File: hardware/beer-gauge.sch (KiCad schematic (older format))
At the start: 19 parts, among them J1 OLED_MODULE, P1 CONN_01X04, P2 CONN_01X04, P3 CONN_01X04, P4 CONN_01X04, U1 ADS1234IPW

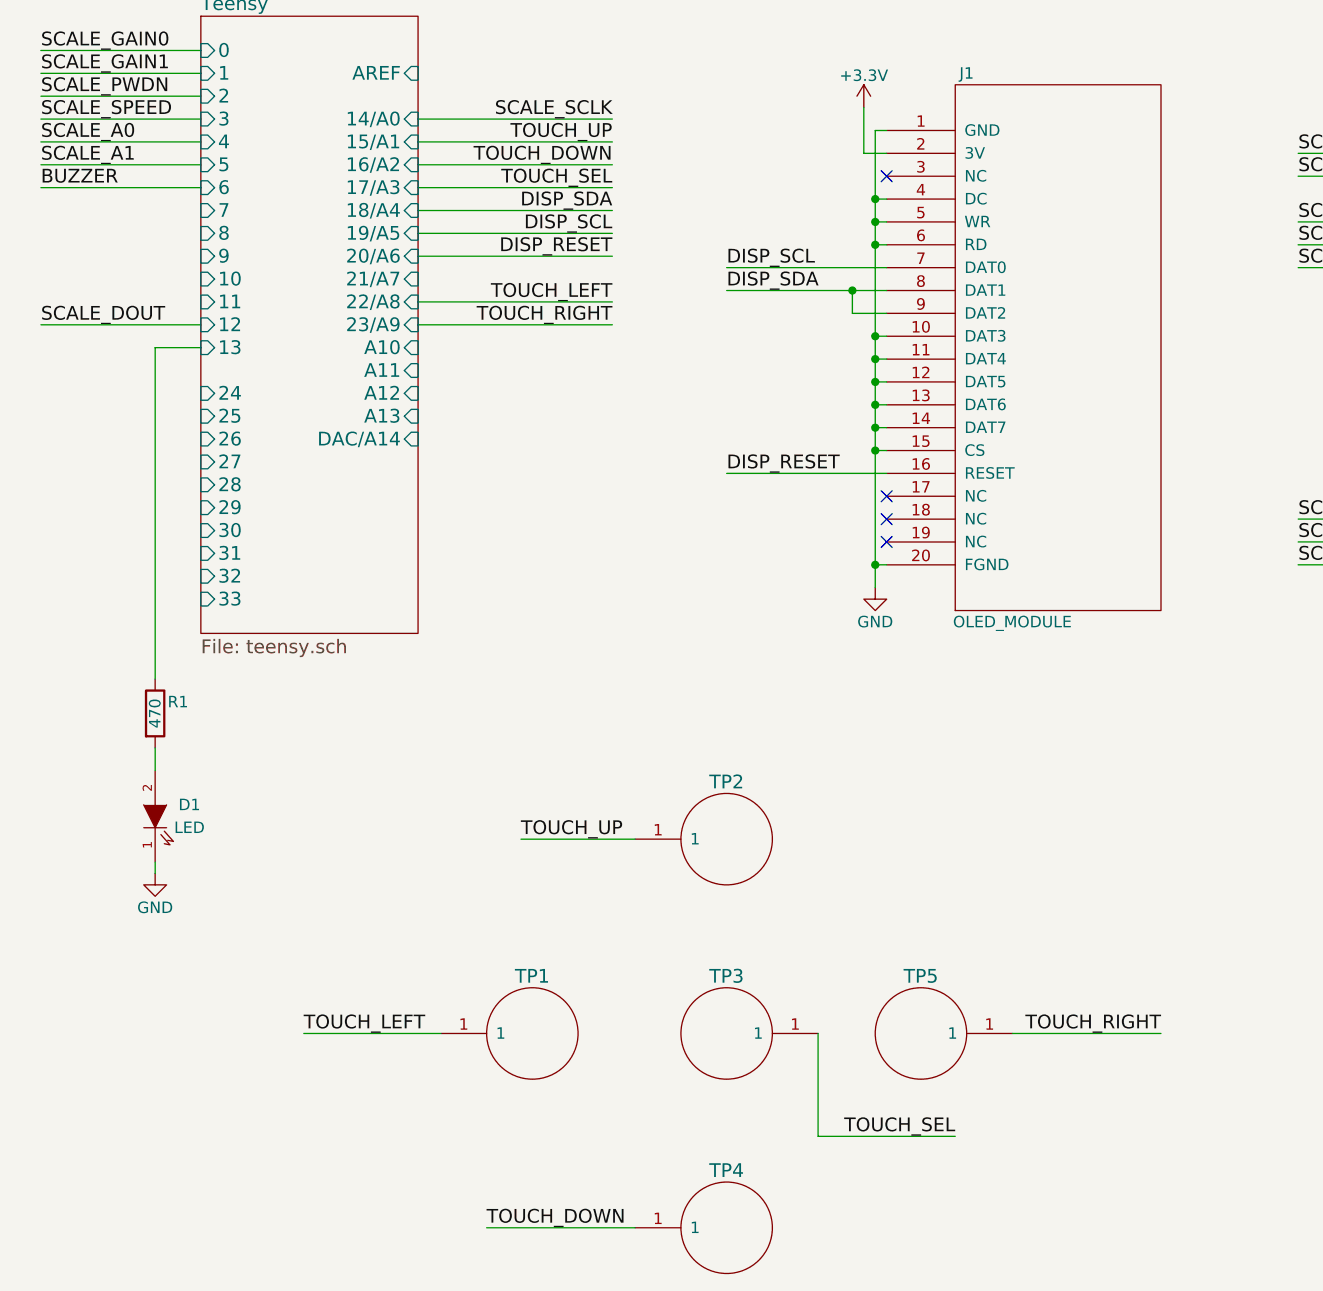
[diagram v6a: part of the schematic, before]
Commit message: Working on capacitive touch pad.  Added footprint for piezo
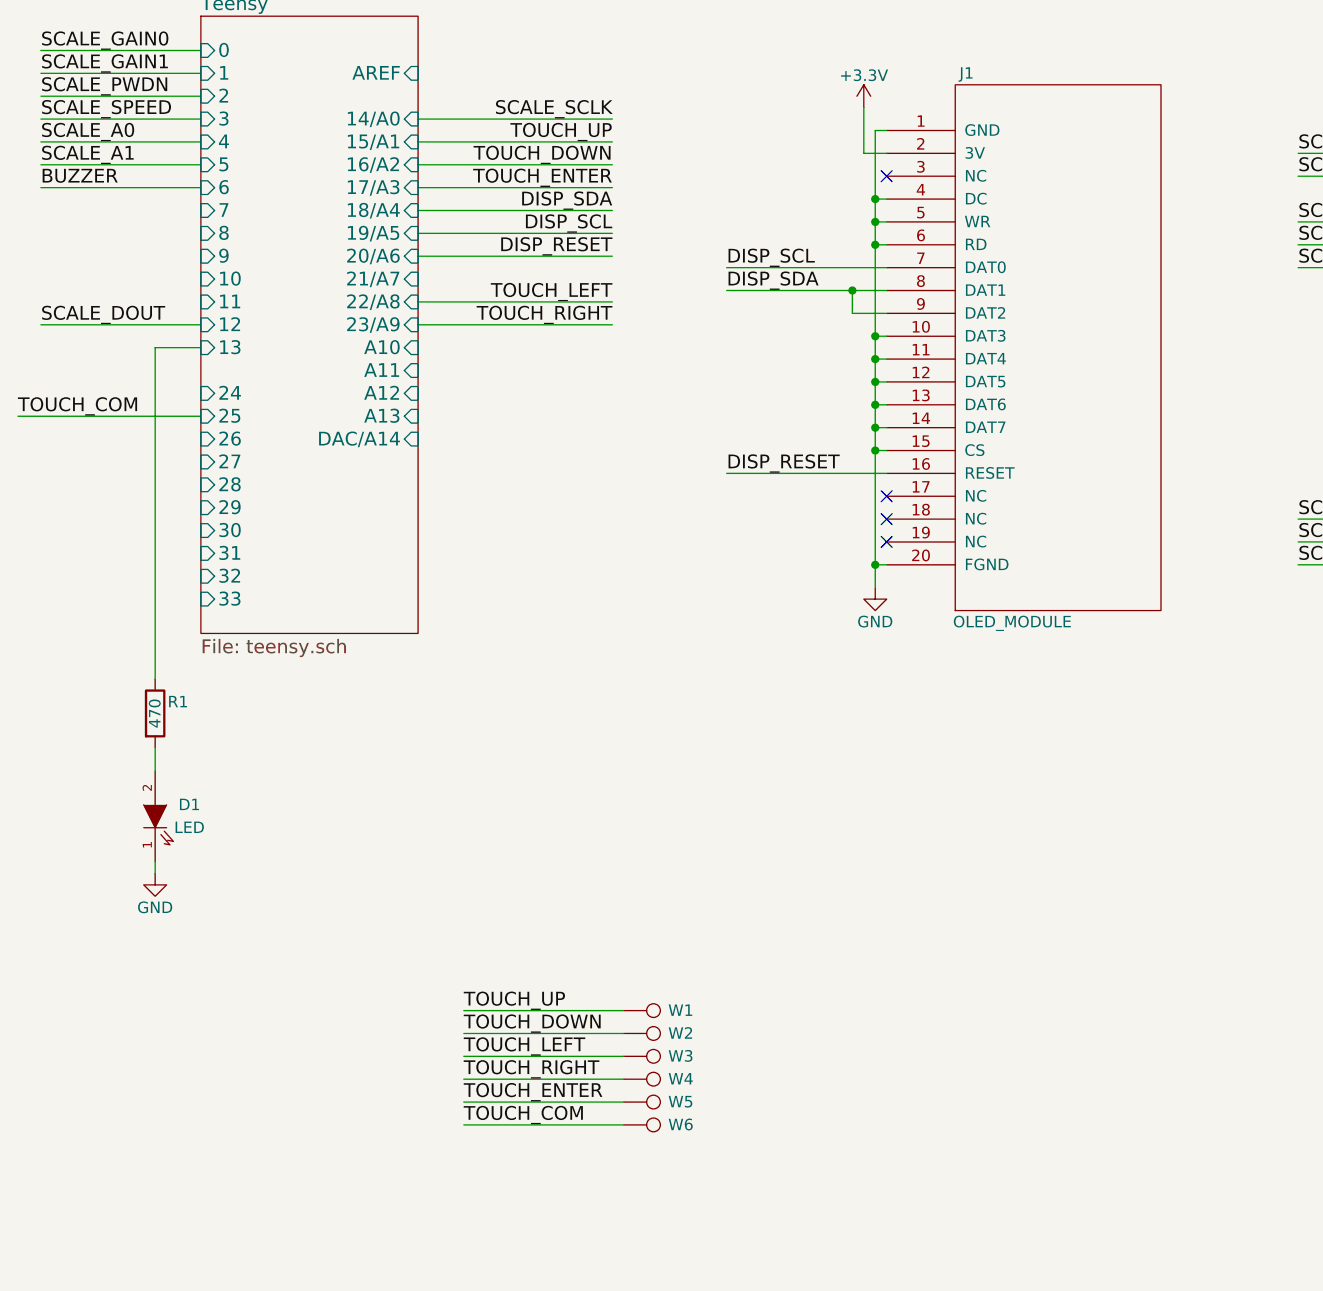
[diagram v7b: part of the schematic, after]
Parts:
- removed TP1, TP2, TP3, TP4, TP5: TOUCH_PAD, symbol TOUCH_PAD
- added W1, W2, W3, W4, W5, W6: TEST_1P, Measurement_Points:Measurement_Point_Round-TH_Small, symbol TEST_1P
- R5: footprint (none) -> Resistors_SMD:R_0603
- SP1: footprint (none) -> footprint:PKMCS
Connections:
- net TOUCH_DOWN: now also W2.1
- net TOUCH_LEFT: now also W3.1
- net TOUCH_RIGHT: now also W4.1
- net TOUCH_UP: now also W1.1
- new net TOUCH_COM: W6.1
- new net TOUCH_ENTER: W5.1
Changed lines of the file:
@@
 Text Label 3600 2650 2    60   ~ 0
 DISP_SDA
-Text Label 2250 6250 0    60   ~ 0
+Text Label 2950 6350 0    60   ~ 0
 TOUCH_LEFT
-Text Label 6000 6250 2    60   ~ 0
+Text Label 2950 6450 0    60   ~ 0
 TOUCH_RIGHT
-Text Label 3200 5400 0    60   ~ 0
+Text Label 2950 6150 0    60   ~ 0
 TOUCH_UP
-Text Label 3050 7100 0    60   ~ 0
+Text Label 2950 6250 0    60   ~ 0
 TOUCH_DOWN
 Text Label 3600 2350 2    60   ~ 0
@@
 Text Label 3600 3150 2    60   ~ 0
 TOUCH_RIGHT
-Text Label 3600 2550 2    60   ~ 0
-TOUCH_SEL
 $Sheet
 S 1800 1800 950  2700
@@
 $EndSheet
 $Comp
-L TOUCH_PAD TP1
-U 1 1 576569ED
-P 3250 6250
-F 0 "TP1" H 3250 6500 60  0000 C CNN
-F 1 "TOUCH_PAD" H 3300 5950 60  0001 C CNN
-F 2 "" H 3250 6250 60  0000 C CNN
-F 3 "" H 3250 6250 60  0000 C CNN
-	1    3250 6250
-	1    0    0    -1
-$EndComp
-Text Label 5100 6700 2    60   ~ 0
-TOUCH_SEL
-$Comp
-L TOUCH_PAD TP3
-U 1 1 57658C3A
-P 4100 6250
-F 0 "TP3" H 4100 6000 60  0000 C CNN
-F 1 "TOUCH_PAD" H 4150 5950 60  0001 C CNN
-F 2 "" H 4100 6250 60  0000 C CNN
-F 3 "" H 4100 6250 60  0000 C CNN
-	1    4100 6250
-	-1   0    0    1
-$EndComp
-$Comp
-L TOUCH_PAD TP5
-U 1 1 57658DCD
-P 4950 6250
-F 0 "TP5" H 4950 6000 60  0000 C CNN
-F 1 "TOUCH_PAD" H 5000 5950 60  0001 C CNN
-F 2 "" H 4950 6250 60  0000 C CNN
-F 3 "" H 4950 6250 60  0000 C CNN
-	1    4950 6250
-	-1   0    0    1
-$EndComp
-$Comp
-L TOUCH_PAD TP2
-U 1 1 57658F39
-P 4100 5400
-F 0 "TP2" H 4100 5650 60  0000 C CNN
-F 1 "TOUCH_PAD" H 4150 5100 60  0001 C CNN
-F 2 "" H 4100 5400 60  0000 C CNN
-F 3 "" H 4100 5400 60  0000 C CNN
-	1    4100 5400
-	1    0    0    -1
-$EndComp
-$Comp
-L TOUCH_PAD TP4
-U 1 1 576590AE
-P 4100 7100
-F 0 "TP4" H 4100 7350 60  0000 C CNN
-F 1 "TOUCH_PAD" H 4150 6800 60  0001 C CNN
-F 2 "" H 4100 7100 60  0000 C CNN
-F 3 "" H 4100 7100 60  0000 C CNN
-	1    4100 7100
-	1    0    0    -1
-$EndComp
-$Comp
 L LED D1
 U 1 1 57679070
@@
 Connection ~ 4750 3700
 Wire Wire Line
-	4500 6250 4500 6700
-Wire Wire Line
-	4500 6700 5100 6700
-Wire Wire Line
-	5350 6250 6000 6250
-Wire Wire Line
-	2250 6250 2850 6250
-Wire Wire Line
-	3200 5400 3700 5400
-Wire Wire Line
-	3050 7100 3700 7100
-Wire Wire Line
-	2750 2550 3600 2550
-Wire Wire Line
 	2750 3150 3600 3150
 Wire Wire Line
@@
 F 0 "SP1" H 9200 6200 50  0000 C CNN
 F 1 "PIEZO" H 9200 5700 50  0000 C CNN
-F 2 "" H 9300 5950 50  0000 C CNN
+F 2 "footprint:PKMCS" H 9300 5950 50  0001 C CNN
 F 3 "" H 9300 5950 50  0000 C CNN
 	1    9300 5950
@@
 F 0 "R5" V 8780 5850 50  0000 C CNN
 F 1 "1k" V 8700 5850 50  0000 C CNN
-F 2 "" V 8630 5850 50  0000 C CNN
+F 2 "Resistors_SMD:R_0603" V 8630 5850 50  0001 C CNN
 F 3 "" H 8700 5850 50  0000 C CNN
 	1    8700 5850
@@
 Wire Wire Line
 	1100 2550 1800 2550
+Text Label 2950 6550 0    60   ~ 0
+TOUCH_ENTER
+Text Label 2950 6650 0    60   ~ 0
+TOUCH_COM
+Text Label 3600 2550 2    60   ~ 0
+TOUCH_ENTER
+Text Label 1000 3550 0    60   ~ 0
+TOUCH_COM
+Wire Wire Line
+	3600 2550 2750 2550
+Wire Wire Line
+	1000 3550 1800 3550
+Wire Wire Line
+	2950 6150 3650 6150
+Wire Wire Line
+	2950 6250 3650 6250
+Wire Wire Line
+	2950 6350 3650 6350
+Wire Wire Line
+	2950 6450 3650 6450
+Wire Wire Line
+	2950 6550 3650 6550
+Wire Wire Line
+	2950 6650 3650 6650
+$Comp
+L TEST_1P W1
+U 1 1 5767B554
+P 3650 6150
+F 0 "W1" V 3650 6400 50  0000 C CNN
+F 1 "TEST_1P" H 3650 6350 50  0001 C CNN
+F 2 "Measurement_Points:Measurement_Point_Round-TH_Small" H 3850 6150 50  0001 C CNN
+F 3 "" H 3850 6150 50  0000 C CNN
+	1    3650 6150
+	0    1    1    0
+$EndComp
+$Comp
+L TEST_1P W2
+U 1 1 5767BE08
+P 3650 6250
+F 0 "W2" V 3650 6500 50  0000 C CNN
+F 1 "TEST_1P" H 3650 6450 50  0001 C CNN
+F 2 "Measurement_Points:Measurement_Point_Round-TH_Small" H 3850 6250 50  0001 C CNN
+F 3 "" H 3850 6250 50  0000 C CNN
+	1    3650 6250
+	0    1    1    0
+$EndComp
+$Comp
+L TEST_1P W3
+U 1 1 5767BF3C
+P 3650 6350
+F 0 "W3" V 3650 6600 50  0000 C CNN
+F 1 "TEST_1P" H 3650 6550 50  0001 C CNN
+F 2 "Measurement_Points:Measurement_Point_Round-TH_Small" H 3850 6350 50  0001 C CNN
+F 3 "" H 3850 6350 50  0000 C CNN
+	1    3650 6350
+	0    1    1    0
+$EndComp
+$Comp
+L TEST_1P W4
+U 1 1 5767C075
+P 3650 6450
+F 0 "W4" V 3650 6700 50  0000 C CNN
+F 1 "TEST_1P" H 3650 6650 50  0001 C CNN
+F 2 "Measurement_Points:Measurement_Point_Round-TH_Small" H 3850 6450 50  0001 C CNN
+F 3 "" H 3850 6450 50  0000 C CNN
+	1    3650 6450
+	0    1    1    0
+$EndComp
+$Comp
+L TEST_1P W5
+U 1 1 5767C386
+P 3650 6550
+F 0 "W5" V 3650 6800 50  0000 C CNN
+F 1 "TEST_1P" H 3650 6750 50  0001 C CNN
+F 2 "Measurement_Points:Measurement_Point_Round-TH_Small" H 3850 6550 50  0001 C CNN
+F 3 "" H 3850 6550 50  0000 C CNN
+	1    3650 6550
+	0    1    1    0
+$EndComp
+$Comp
+L TEST_1P W6
+U 1 1 5767C4C3
+P 3650 6650
+F 0 "W6" V 3650 6900 50  0000 C CNN
+F 1 "TEST_1P" H 3650 6850 50  0001 C CNN
+F 2 "Measurement_Points:Measurement_Point_Round-TH_Small" H 3850 6650 50  0001 C CNN
+F 3 "" H 3850 6650 50  0000 C CNN
+	1    3650 6650
+	0    1    1    0
+$EndComp
 $EndSCHEMATC

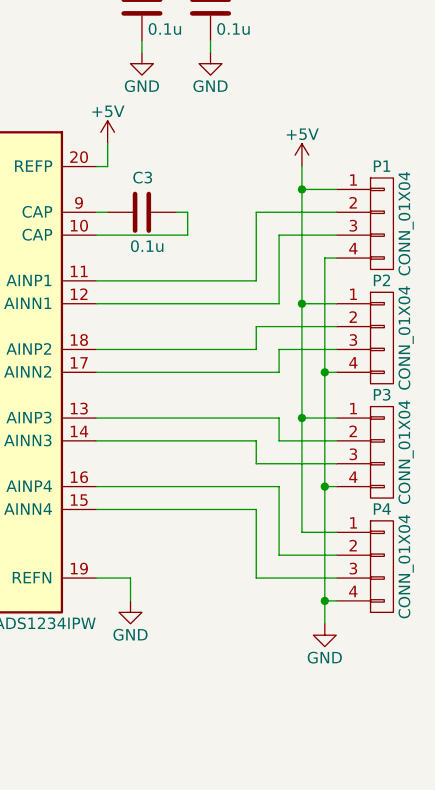
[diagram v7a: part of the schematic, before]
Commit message: Added footprint for coin cell battery holder and RJ10 jack
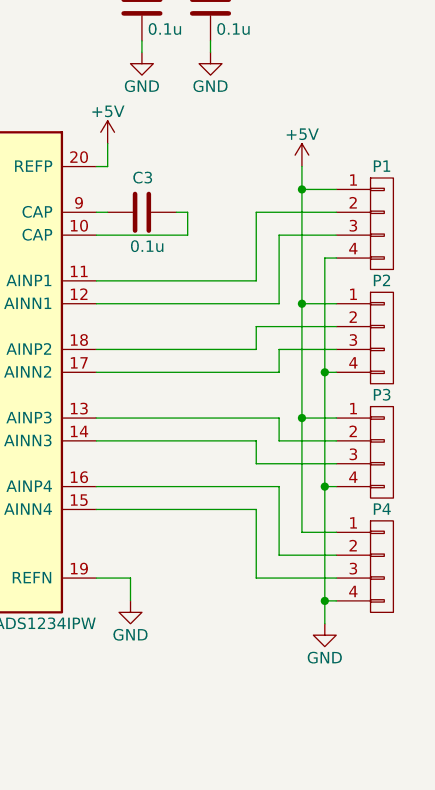
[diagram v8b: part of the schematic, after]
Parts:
- P1, P2, P3, P4: footprint (none) -> footprint:0855135016
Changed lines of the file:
@@
 P 9950 2650
 F 0 "P1" H 9950 2900 50  0000 C CNN
-F 1 "CONN_01X04" V 10050 2650 50  0000 C CNN
-F 2 "" H 9950 2650 50  0000 C CNN
+F 1 "CONN_01X04" V 10050 2650 50  0001 C CNN
+F 2 "footprint:0855135016" H 9950 2650 50  0001 C CNN
 F 3 "" H 9950 2650 50  0000 C CNN
 	1    9950 2650
@@
 P 9950 3150
 F 0 "P2" H 9950 3400 50  0000 C CNN
-F 1 "CONN_01X04" V 10050 3150 50  0000 C CNN
-F 2 "" H 9950 3150 50  0000 C CNN
+F 1 "CONN_01X04" V 10050 3150 50  0001 C CNN
+F 2 "footprint:0855135016" H 9950 3150 50  0001 C CNN
 F 3 "" H 9950 3150 50  0000 C CNN
 	1    9950 3150
@@
 P 9950 3650
 F 0 "P3" H 9950 3900 50  0000 C CNN
-F 1 "CONN_01X04" V 10050 3650 50  0000 C CNN
-F 2 "" H 9950 3650 50  0000 C CNN
+F 1 "CONN_01X04" V 10050 3650 50  0001 C CNN
+F 2 "footprint:0855135016" H 9950 3650 50  0001 C CNN
 F 3 "" H 9950 3650 50  0000 C CNN
 	1    9950 3650
@@
 P 9950 4150
 F 0 "P4" H 9950 4400 50  0000 C CNN
-F 1 "CONN_01X04" V 10050 4150 50  0000 C CNN
-F 2 "" H 9950 4150 50  0000 C CNN
+F 1 "CONN_01X04" V 10050 4150 50  0001 C CNN
+F 2 "footprint:0855135016" H 9950 4150 50  0001 C CNN
 F 3 "" H 9950 4150 50  0000 C CNN
 	1    9950 4150
